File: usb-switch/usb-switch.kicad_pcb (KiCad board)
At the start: 2 copper layers, 114.3 x 134.6 mm, 136 parts, among them J1 USB_C_Receptacle, J2 USB_C_Receptacle, J3 USB_C_Receptacle, J4 USB_C_Receptacle, J5 USB_C_Receptacle, J6 USB_C_Receptacle, J7 USB_C_Receptacle, J8 USB_C_Receptacle, U1 LTC4317, U10 TUSB8043AIRGCR, U11 FUSB307BMPX, U12 HD3SS3212IRKSR, U13 TUSB8043AIRGCR, U14 FUSB307BMPX, U15 HD3SS3212IRKSR, U16 TUSB8043AIRGCR, U17 FUSB307BMPX, U18 HD3SS3212IRKSR, U19 TUSB8043AIRGCR, U2 LTC4317, U20 max4999etj+, U21 HD3SS3412RUAR, U22 TCA9534, U23 HD3SS3212IRKSR, U24 HD3SS3212IRKSR, U25 FUSB307BMPX, U26 max4999etj+, U27 HD3SS3412RUAR, U28 TCA9534, U29 HD3SS3212IRKSR, U3 PCA9537, U30 HD3SS3212IRKSR, U31 FUSB307BMPX, U32 max4999etj+, U33 HD3SS3412RUAR, U34 TCA9534, U35 HD3SS3212IRKSR, U36 HD3SS3212IRKSR, U37 FUSB307BMPX, U38 max4999etj+, U39 HD3SS3412RUAR, U4 RP2040, U40 TCA9534, U41 HD3SS3212IRKSR, U42 HD3SS3212IRKSR, U43 FUSB307BMPX, U5 LTC4317, U6 PCA9537, U7 LTC4317, U8 FUSB307BMPX, U9 HD3SS3212IRKSR, X1 ASDMB-24MHz

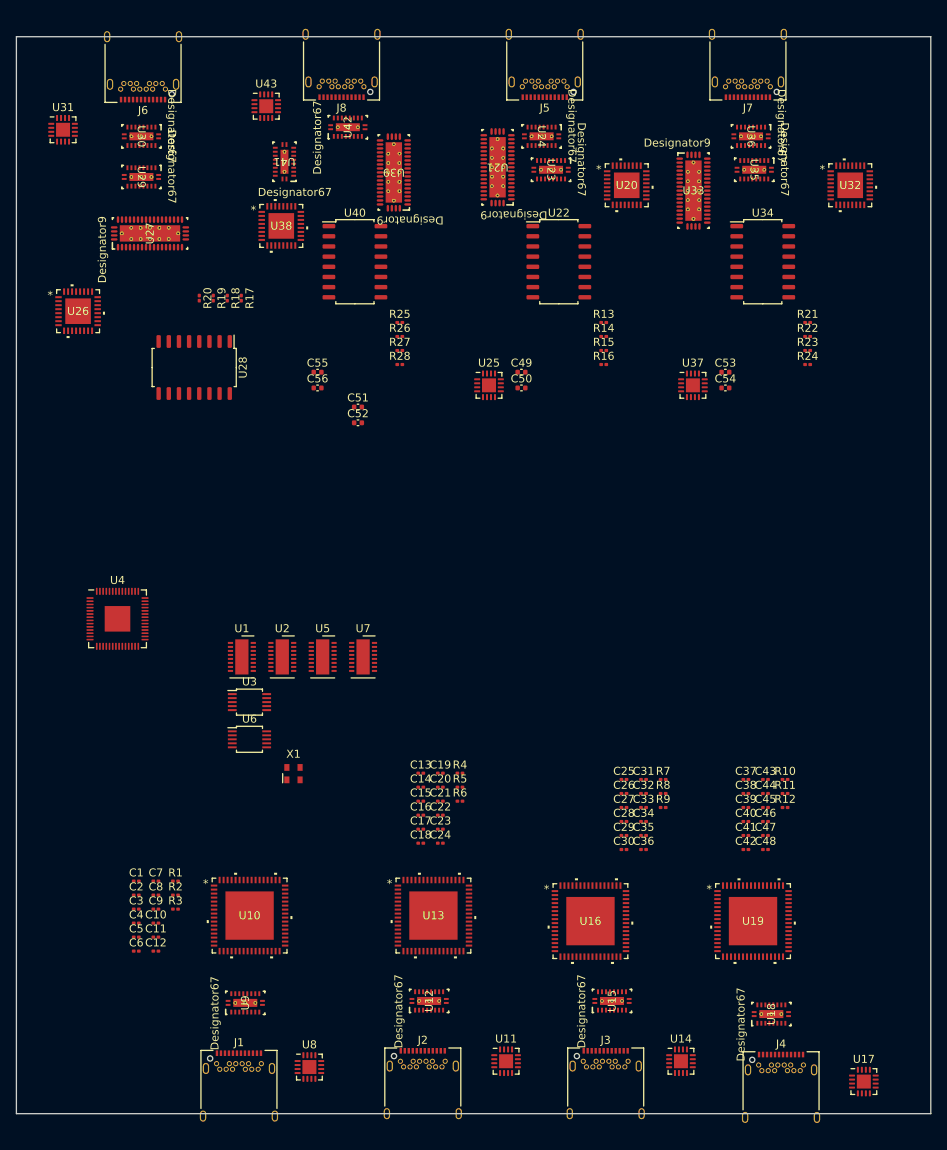
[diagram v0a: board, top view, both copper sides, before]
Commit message: Added some missing I2C and interrupt connections, further organizing of PCB layout
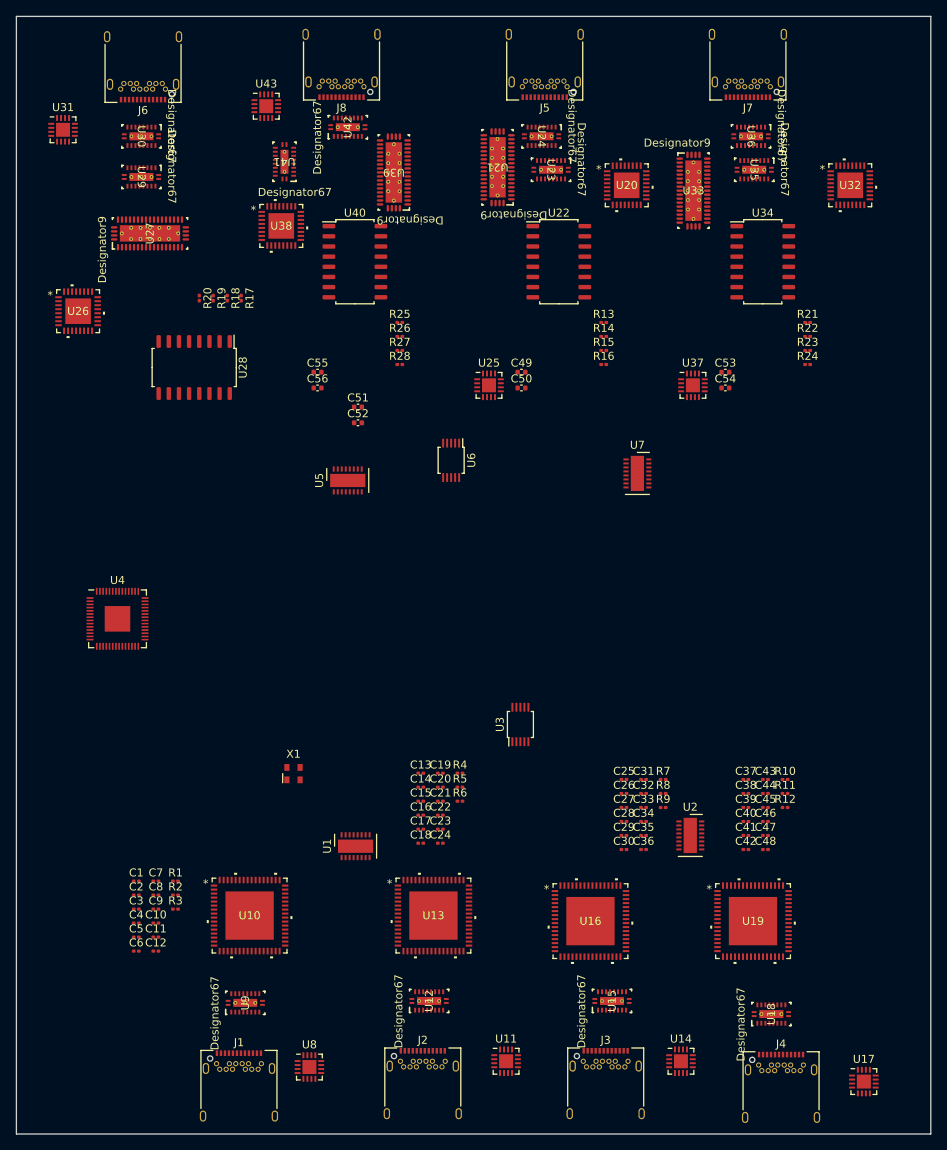
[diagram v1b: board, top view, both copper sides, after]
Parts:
- moved U2 55.7 mm to (157.9, 125.2)
- moved U6 43.0 mm to (128.0, 78.3), turned to -90 degrees
- moved U7 41.3 mm to (151.3, 80.0)
- moved U3 34.0 mm to (136.7, 111.4), turned to 90 degrees
- moved U1 27.6 mm to (116.1, 126.6), turned to 90 degrees
- moved U5 22.3 mm to (115.1, 80.9), turned to 90 degrees
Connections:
- U22 pad 13: /downstream_port/CONTROL.INT -> /DFPCTL1.INT
- U22 pad 14: /downstream_port/CONTROL.SCL -> /DFPCTL1.SCL
- U22 pad 15: /downstream_port/CONTROL.SDA -> /DFPCTL1.SDA
- U25 pad 11: /downstream_port/CONTROL.SCL -> /DFPCTL1.SCL
- U25 pad 12: /downstream_port/CONTROL.SDA -> /DFPCTL1.SDA
- U28 pad 13: /downstream_port1/CONTROL.INT -> /DFPCTL2.INT
- U28 pad 14: /downstream_port1/CONTROL.SCL -> /DFPCTL2.SCL
- U28 pad 15: /downstream_port1/CONTROL.SDA -> /DFPCTL2.SDA
- U31 pad 11: /downstream_port1/CONTROL.SCL -> /DFPCTL2.SCL
- U31 pad 12: /downstream_port1/CONTROL.SDA -> /DFPCTL2.SDA
- U34 pad 13: /downstream_port2/CONTROL.INT -> /DFPCTL3.INT
- U34 pad 14: /downstream_port2/CONTROL.SCL -> /DFPCTL3.SCL
- U34 pad 15: /downstream_port2/CONTROL.SDA -> /DFPCTL3.SDA
- U37 pad 11: /downstream_port2/CONTROL.SCL -> /DFPCTL3.SCL
- U37 pad 12: /downstream_port2/CONTROL.SDA -> /DFPCTL3.SDA
- U40 pad 13: /downstream_port3/CONTROL.INT -> /DFPCTL4.INT
- U40 pad 14: /downstream_port3/CONTROL.SCL -> /DFPCTL4.SCL
- U40 pad 15: /downstream_port3/CONTROL.SDA -> /DFPCTL4.SDA
- U43 pad 11: /downstream_port3/CONTROL.SCL -> /DFPCTL4.SCL
- U43 pad 12: /downstream_port3/CONTROL.SDA -> /DFPCTL4.SDA
- U5 pad 11: unconnected-(U5-SDAOUT2-Pad11) -> /DFPCTL2.SDA
- U5 pad 12: unconnected-(U5-SDAIN-Pad12) -> /SDA
- U5 pad 13: unconnected-(U5-SDAOUT1-Pad13) -> /DFPCTL1.SDA
- U5 pad 14: unconnected-(U5-SCLOUT1-Pad14) -> /DFPCTL1.SCL
- U5 pad 15: unconnected-(U5-SCLIN-Pad15) -> /SCL
- U5 pad 16: unconnected-(U5-SCLOUT2-Pad16) -> /DFPCTL2.SCL
- U6 pad 1: unconnected-(U6-IO0-Pad1) -> /DFPCTL1.INT
- U6 pad 2: unconnected-(U6-IO1-Pad2) -> /DFPCTL2.INT
- U6 pad 3: unconnected-(U6-IO2-Pad3) -> /DFPCTL3.INT
- U6 pad 4: unconnected-(U6-IO3-Pad4) -> /DFPCTL4.INT
- U6 pad 8: unconnected-(U6-SCL-Pad8) -> /SCL
- U6 pad 9: unconnected-(U6-SDA-Pad9) -> /SDA
- U7 pad 11: unconnected-(U7-SDAOUT2-Pad11) -> /DFPCTL4.SDA
- U7 pad 12: unconnected-(U7-SDAIN-Pad12) -> /SDA
- U7 pad 13: unconnected-(U7-SDAOUT1-Pad13) -> /DFPCTL3.SDA
- U7 pad 14: unconnected-(U7-SCLOUT1-Pad14) -> /DFPCTL3.SCL
- U7 pad 15: unconnected-(U7-SCLIN-Pad15) -> /SCL
- U7 pad 16: unconnected-(U7-SCLOUT2-Pad16) -> /DFPCTL4.SCL
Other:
- board size 114.3 x 134.6 mm -> 114.3 x 139.7 mm
